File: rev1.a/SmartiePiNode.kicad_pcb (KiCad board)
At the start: 2 copper layers, 71.7 x 55 mm, 62 parts, among them CN1 USBMICROb, CN2 SWD, CN3 SX1238_TRX_HEADER, CN4 VIN, SW1 SW_PUSH, U1 ISL91127IR, U2 STM32L052_LQFP48, X1 abm10, X2 ABS25-32.768KHZ-6-T

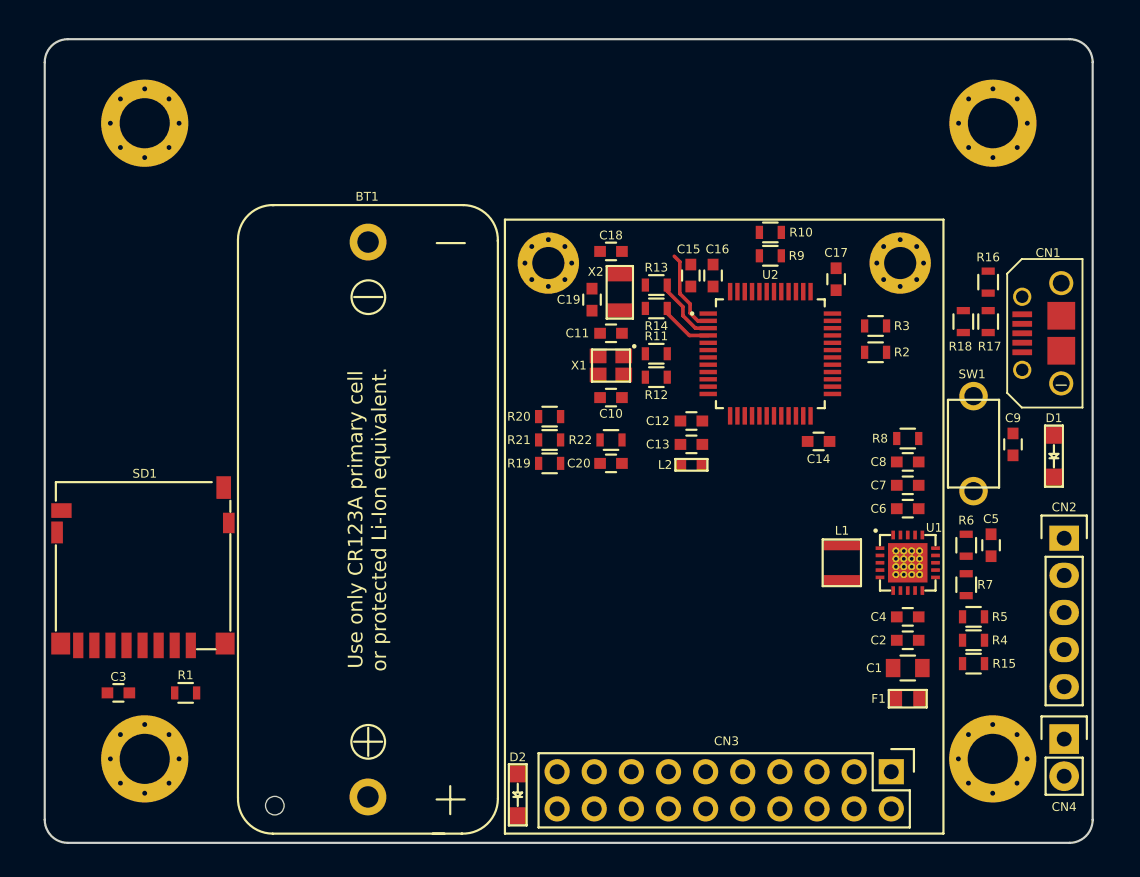
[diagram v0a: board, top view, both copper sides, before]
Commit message: starting psu/vcc and ground traces.
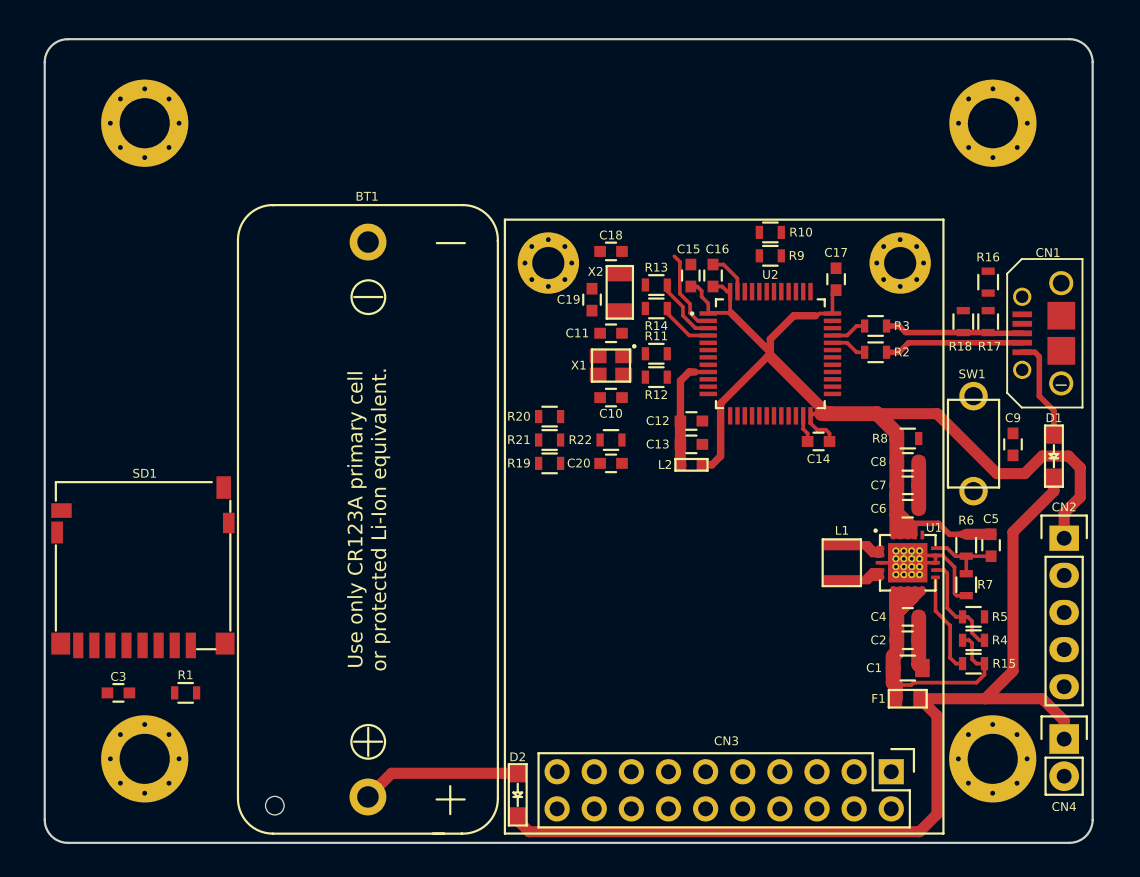
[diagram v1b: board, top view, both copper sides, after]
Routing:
- net /+3V3: track 0.00 -> 86.5 mm
- net Net-(CN4-Pad1): track 0.00 -> 67.0 mm
- net /+VIN: track 0.37 -> 31.3 mm
- net GND: track 0.00 -> 21.4 mm
- net /+VBAT: track 0.00 -> 10.9 mm
- net Net-(CN1-Pad2): track 0.00 -> 9.55 mm
- net Net-(CN1-Pad3): track 0.00 -> 9.49 mm
- net /+VDDA: track 0.00 -> 7.91 mm
- net Net-(R4-Pad1): track 0.00 -> 7.21 mm
- net /+VUSB: track 0.00 -> 7.04 mm
- net Net-(R15-Pad1): track 0.00 -> 6.93 mm
- net Net-(L1-Pad1): track 0.00 -> 5.68 mm
- net Net-(C5-Pad2): track 0.00 -> 5.23 mm
- net Net-(L1-Pad2): track 0.00 -> 4.87 mm
- net /USB_DM: track 0.00 -> 2.47 mm
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
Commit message: figuring out traces for trx and power lines.
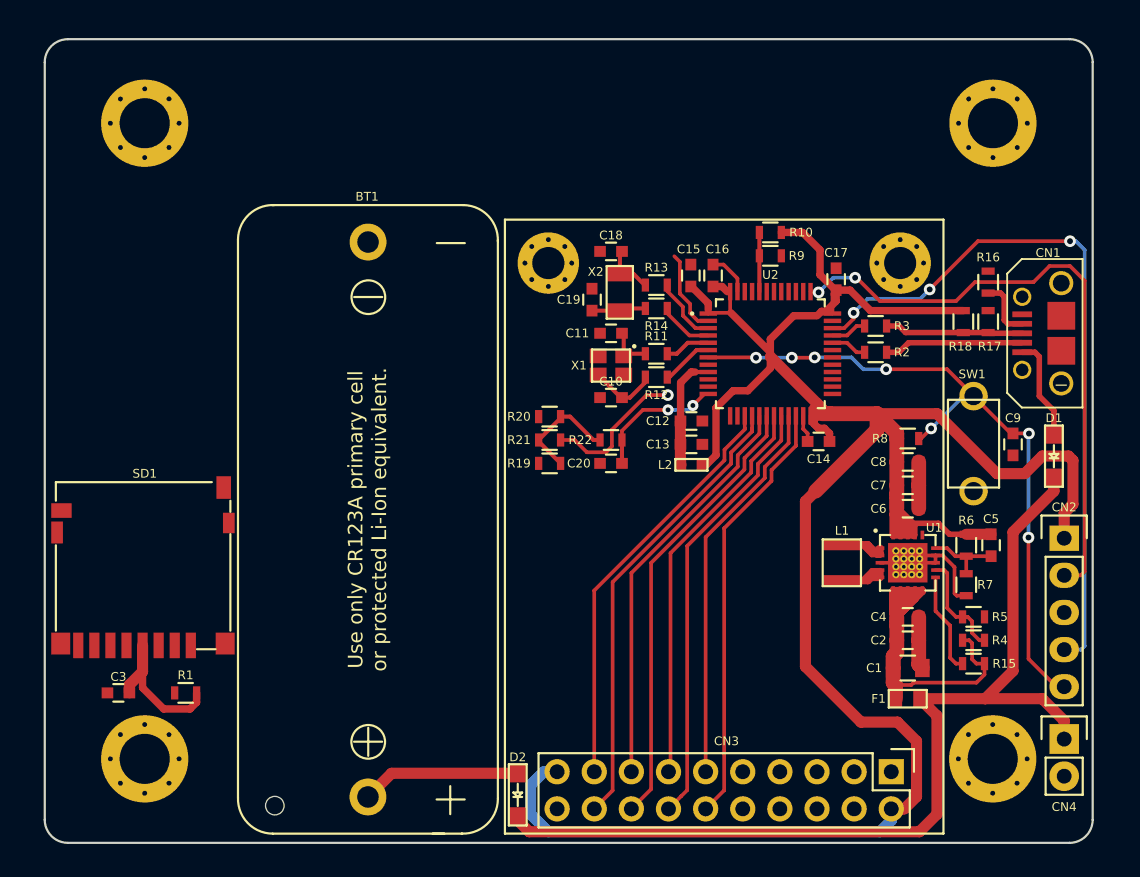
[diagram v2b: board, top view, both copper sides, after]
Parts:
- turned C10 to 0 degrees
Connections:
- U2 pad 11: Net-(U2-Pad11) -> /VSENSE
- U2 pad 12: Net-(U2-Pad12) -> /VMEASURE
- U2 pad 15: Net-(U2-Pad15) -> /TRX_MODE
- U2 pad 16: Net-(U2-Pad16) -> /TRX_TXEN
- U2 pad 17: Net-(U2-Pad17) -> /TRX_RXEN
- U2 pad 18: Net-(U2-Pad18) -> /TRX_RXTX
- U2 pad 19: Net-(U2-Pad19) -> /TRX_RESET
- U2 pad 20: Net-(U2-Pad20) -> /TRX_DIO0
- U2 pad 21: Net-(U2-Pad21) -> /TRX_DIO1
- U2 pad 22: Net-(U2-Pad22) -> /TRX_DIO2
- U2 pad 25: Net-(U2-Pad25) -> /TRX_DIO5
- U2 pad 29: Net-(U2-Pad29) -> /SPI2_NSS_TRX
- U2 pad 38: Net-(U2-Pad38) -> /USB_RENUMn
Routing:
- net /+3V3: track 86.5 -> 183.1 mm
- net /SWDIO: track 0.00 -> 48.8 mm, vias 0 -> 3
- net /NRST: track 0.00 -> 47.7 mm, vias 0 -> 7
- net /SWCLK: track 0.00 -> 42.7 mm, vias 0 -> 2
- net /TRX_TXEN: track 0.00 -> 31.4 mm
- net /TRX_RXTX: track 0.00 -> 30.7 mm
- net /TRX_DIO0: track 0.00 -> 30.1 mm
- net /TRX_DIO2: track 0.00 -> 29.4 mm
- net /TRX_MODE: track 0.00 -> 28.6 mm
- net /TRX_RXEN: track 0.00 -> 28.0 mm
- net /TRX_RESET: track 0.00 -> 27.1 mm
- net /TRX_DIO1: track 0.00 -> 26.7 mm
- net /VSENSE: track 0.00 -> 9.98 mm, vias 0 -> 1
- net /VMEASURE: track 0.00 -> 9.17 mm, vias 0 -> 2
- net Net-(R19-Pad2): track 0.00 -> 7.81 mm
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
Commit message: finished routing trx
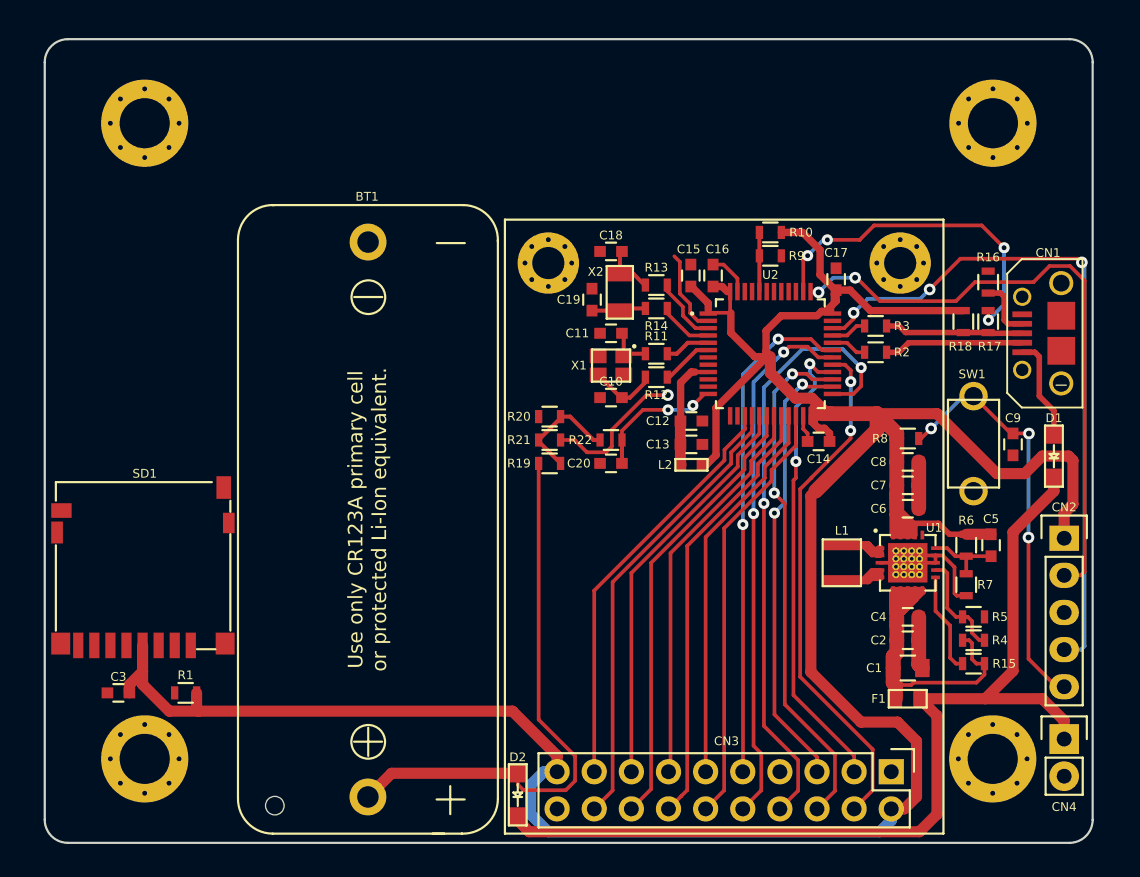
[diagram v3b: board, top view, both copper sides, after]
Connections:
- U2 pad 30: Net-(U2-Pad30) -> /TRX_DIO4
- U2 pad 31: Net-(U2-Pad31) -> /TRX_DIO3
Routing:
- net /TRX_DIO5: track 0.00 -> 42.0 mm, vias 0 -> 2
- net /TRX_DIO4: track 0.00 -> 36.7 mm, vias 0 -> 2
- net /SPI2_NSS_TRX: track 0.00 -> 35.4 mm, vias 0 -> 2
- net /SPI2_MISO: track 0.00 -> 35.4 mm, vias 0 -> 2
- net /TRX_DIO3: track 0.00 -> 34.6 mm, vias 0 -> 2
- net /SPI2_MOSI: track 0.00 -> 32.2 mm, vias 0 -> 2
- net /SPI2_SCK: track 0.00 -> 30.6 mm, vias 0 -> 2
- net /+3V3: track 183.1 -> 211.7 mm
- net /+VBAT: track 10.9 -> 38.8 mm
- net /USB_RENUMn: track 0.00 -> 23.6 mm, vias 0 -> 4
- net /NRST: track 47.7 -> 28.5 mm, vias 7 -> 3
- net /SWDIO: track 48.8 -> 47.2 mm

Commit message: finished ground and initial net traces
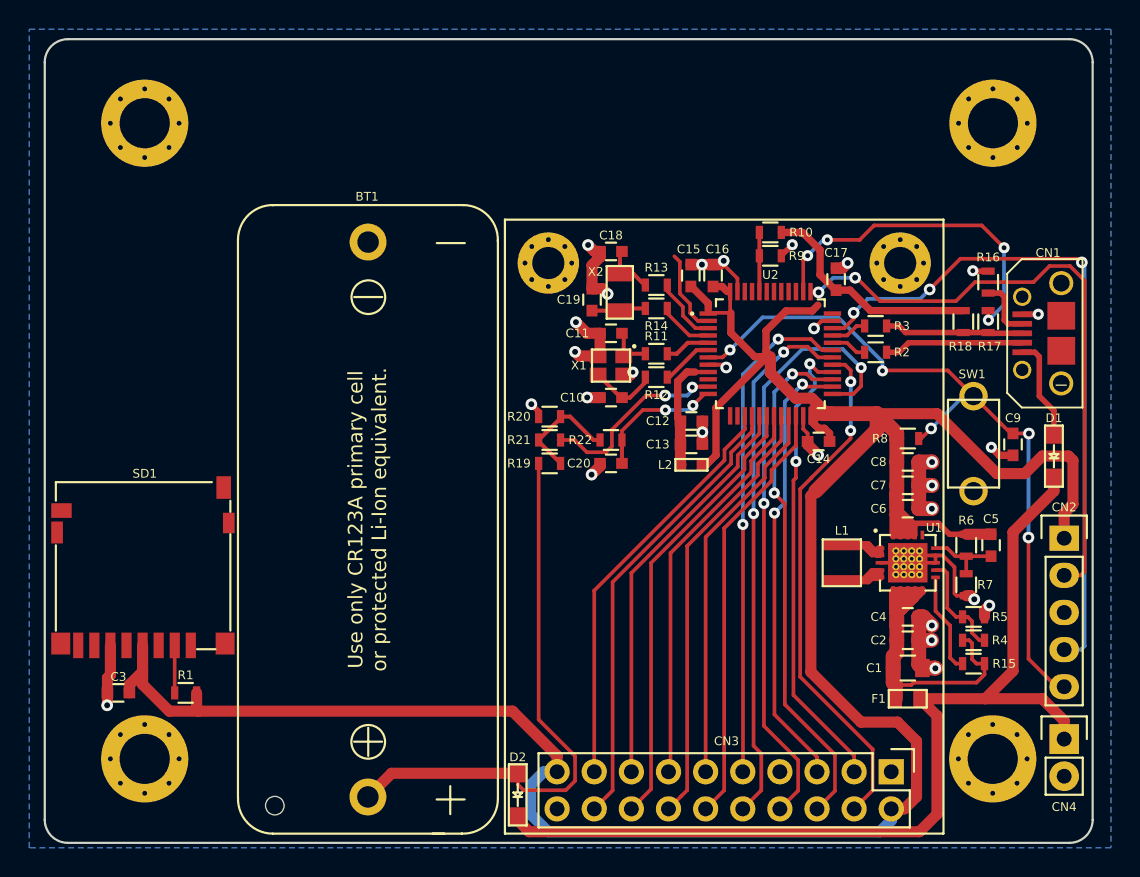
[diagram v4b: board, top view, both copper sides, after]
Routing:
- net GND: track 21.4 -> 61.2 mm, vias 0 -> 28
- net /NRST: track 28.5 -> 50.4 mm, vias 3 -> 5
- net /+3V3: track 211.7 -> 206.8 mm
- net /SPI2_NSS_SDCARD: track 0.00 -> 3.25 mm
- net /VSENSE: track 9.98 -> 13.1 mm, vias 1 -> 2
- added copper zone on B.Cu, net GND

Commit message: more routing of trx and sd card
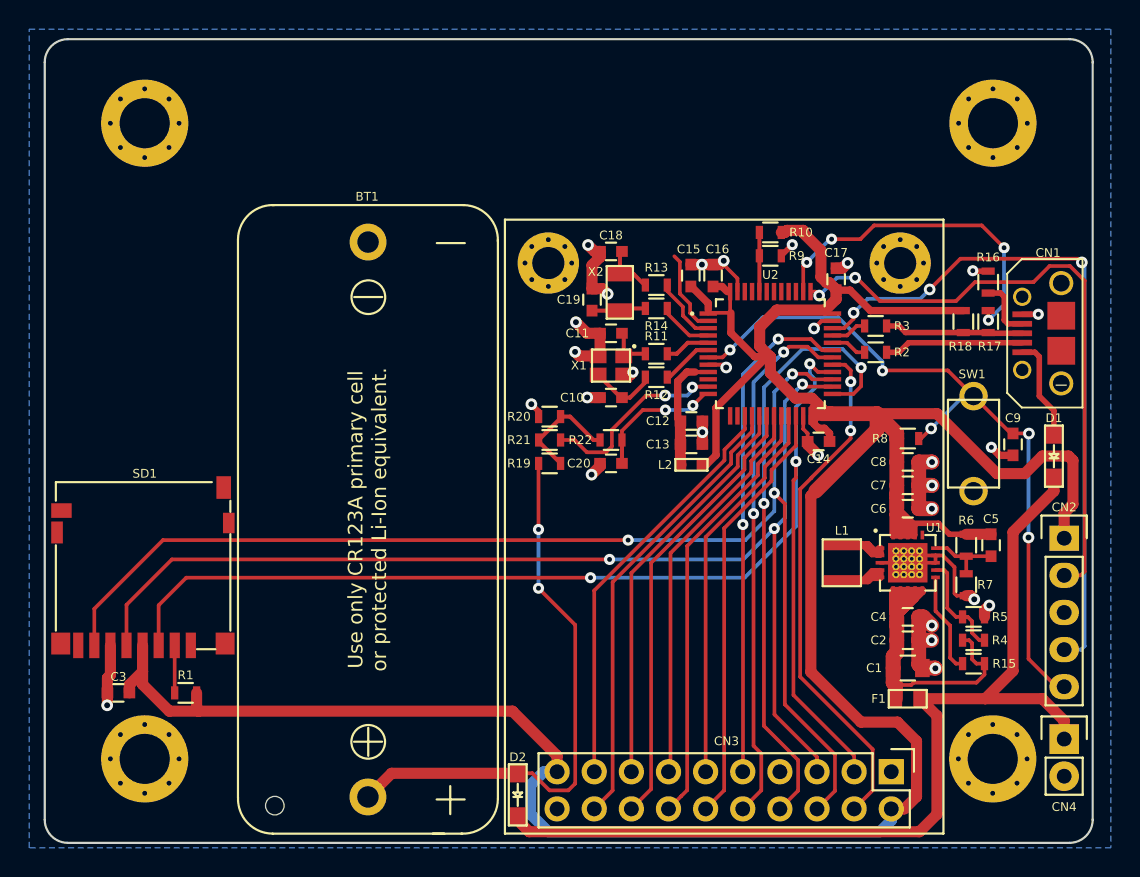
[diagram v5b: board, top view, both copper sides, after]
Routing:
- net /SPI2_MISO: track 35.4 -> 88.4 mm, vias 2 -> 3
- net /SPI2_MOSI: track 32.2 -> 85.2 mm, vias 2 -> 3
- net /SPI2_SCK: track 30.6 -> 79.9 mm, vias 2 -> 3
- net /+3V3: track 206.8 -> 210.0 mm
- net /+VBAT: track 38.8 -> 38.5 mm, vias 0 -> 2

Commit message: everything routed except sensor io header
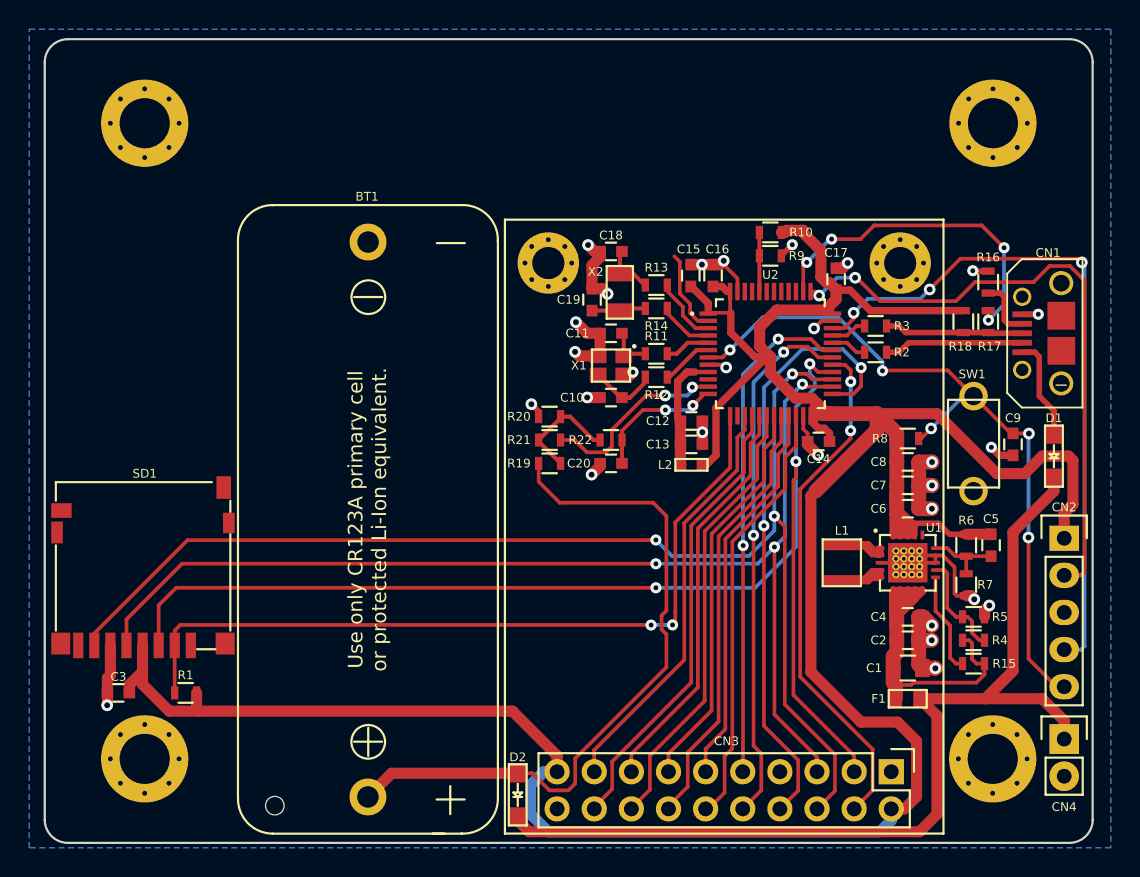
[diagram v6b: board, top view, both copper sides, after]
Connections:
- U2 pad 13: Net-(U2-Pad13) -> /SPI2_NSS_SDCARD
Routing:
- net /SPI2_NSS_SDCARD: track 3.25 -> 54.4 mm, vias 0 -> 2
- net /+VBAT: track 38.5 -> 47.7 mm, vias 2 -> 0
- net /SPI2_SCK: track 79.9 -> 78.8 mm
- net /SPI2_MISO: track 88.4 -> 87.5 mm
- net /SPI2_MOSI: track 85.2 -> 86.0 mm
- net /+3V3: track 210.0 -> 210.8 mm

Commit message: created net for sensor gpio header
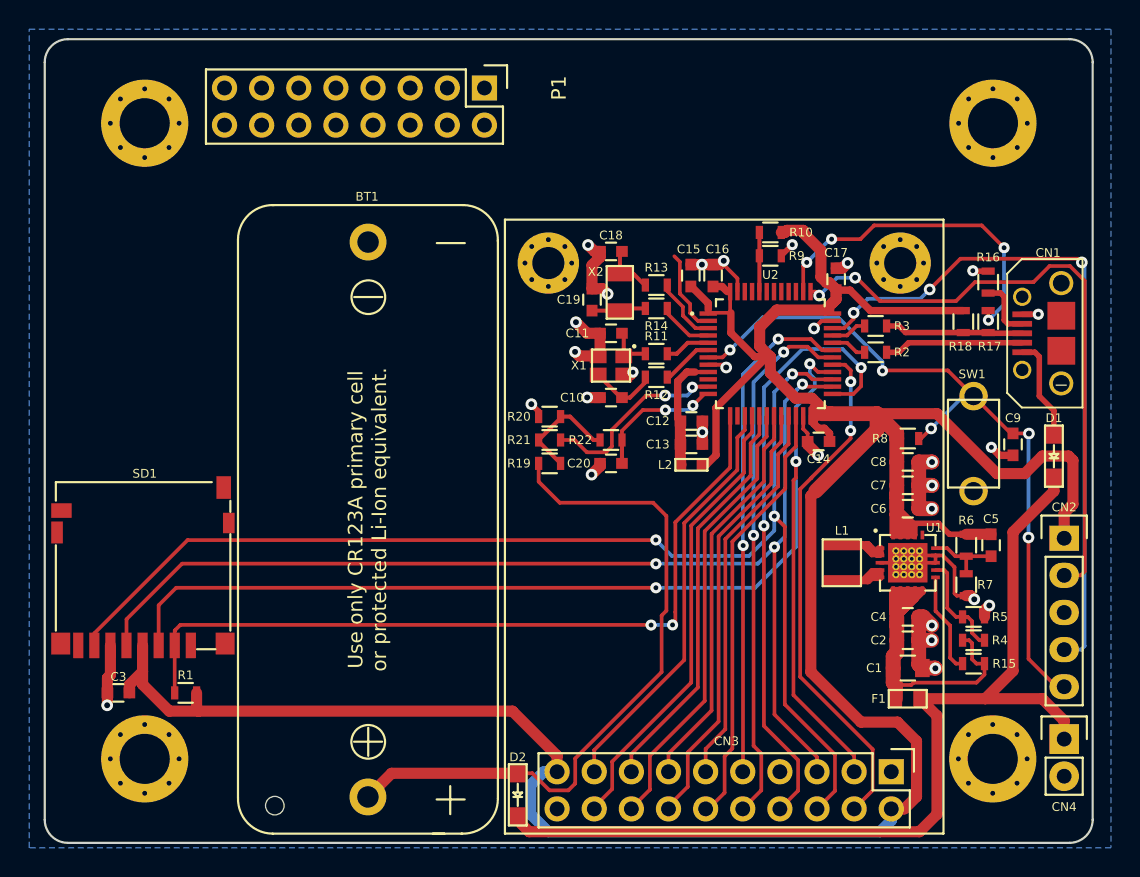
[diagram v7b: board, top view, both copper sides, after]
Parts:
- added P1: SENSOR_GPIO, Pin_Headers:Pin_Header_Straight_2x08, F.Cu at (129.1, 99.0)
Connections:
- U2 pad 10: Net-(U2-Pad10) -> /GPIO_2
- U2 pad 14: Net-(U2-Pad14) -> /GPIO_1
- U2 pad 2: Net-(U2-Pad2) -> /GPIO_3
- U2 pad 39: Net-(U2-Pad39) -> /GPIO_10
- U2 pad 40: Net-(U2-Pad40) -> /GPIO_9
- U2 pad 41: Net-(U2-Pad41) -> /GPIO_8
- U2 pad 42: Net-(U2-Pad42) -> /GPIO_7
- U2 pad 43: Net-(U2-Pad43) -> /GPIO_6
- U2 pad 45: Net-(U2-Pad45) -> /GPIO_5
- U2 pad 46: Net-(U2-Pad46) -> /GPIO_4
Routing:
- net /+VBAT: track 47.7 -> 38.8 mm
- net GND: track 61.2 -> 69.9 mm
- net Net-(U2-Pad2): track 5.80 -> 0.00 mm
- net /GPIO_3: track 0.00 -> 5.80 mm

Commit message: finished routing of rev1.a
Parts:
- removed P1: SENSOR_GPIO, Pin_Headers:Pin_Header_Straight_2x08
- added CN5: SENSOR_GPIO, Pin_Headers:Pin_Header_Straight_2x08, F.Cu at (130.1, 98.3)
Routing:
- net /SPI2_SCK: track 78.8 -> 135.1 mm
- net /SPI2_MOSI: track 86.0 -> 139.7 mm
- net /SPI2_MISO: track 87.5 -> 140.5 mm
- net /GPIO_1: track 0.00 -> 51.5 mm, vias 0 -> 2
- net /GPIO_10: track 0.00 -> 48.3 mm, vias 0 -> 2
- net /GPIO_2: track 0.00 -> 43.0 mm, vias 0 -> 2
- net /GPIO_7: track 0.00 -> 37.5 mm, vias 0 -> 2
- net /GPIO_9: track 0.00 -> 37.3 mm, vias 0 -> 2
- net /GPIO_5: track 0.00 -> 36.9 mm
- net /GPIO_8: track 0.00 -> 36.7 mm, vias 0 -> 2
- net /GPIO_6: track 0.00 -> 34.9 mm
- net /GPIO_4: track 0.00 -> 34.9 mm
- net /GPIO_3: track 5.80 -> 39.2 mm
- net /+3V3: track 210.8 -> 237.8 mm
- net GND: track 69.9 -> 60.8 mm
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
